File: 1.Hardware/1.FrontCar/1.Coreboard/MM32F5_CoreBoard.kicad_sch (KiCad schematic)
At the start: 74 parts, among them J2 USB-Type-C, J6 SH1.0_2P, U3 CH343P

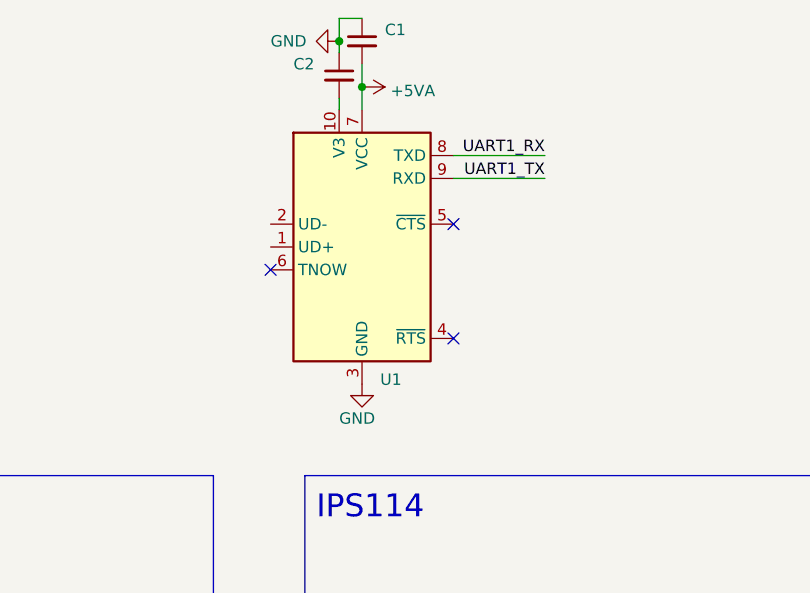
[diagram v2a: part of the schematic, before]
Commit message: 删除遗漏芯片
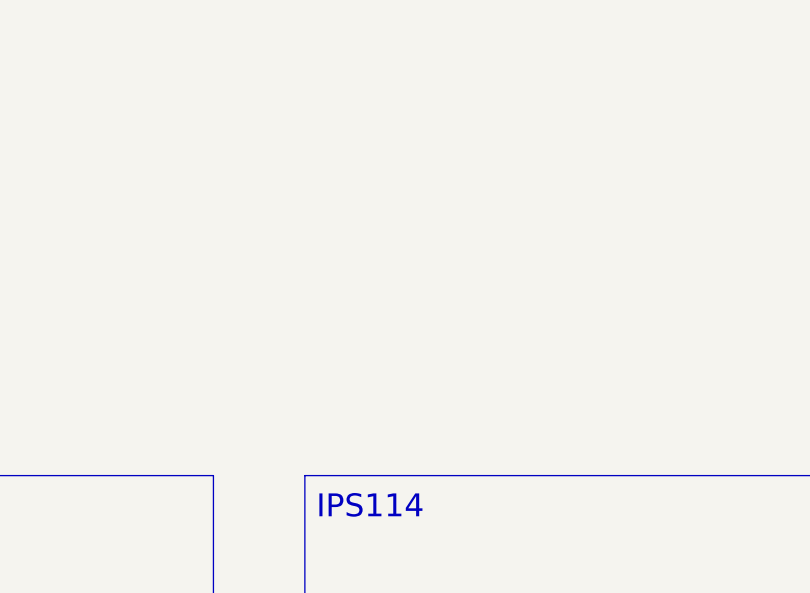
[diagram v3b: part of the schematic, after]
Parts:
- removed C1, C2: (no value), symbol Device:C_Small
- removed U1: (no value), symbol Interface_USB:CH340E
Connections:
- no-connect marks 23 -> 20
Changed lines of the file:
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@@
   (junction (at 69.85 104.14) (diameter 0) (color 0 0 0 0)
   )
-  (junction (at 293.37 -26.67) (diameter 0) (color 0 0 0 0)
-  )
   (junction (at 53.34 30.48) (diameter 0) (color 0 0 0 0)
   )
@@
   (junction (at 85.09 127) (diameter 0) (color 0 0 0 0)
   )
-  (junction (at 290.83 -31.75) (diameter 0) (color 0 0 0 0)
-  )
   (junction (at 193.04 45.72) (diameter 0) (color 0 0 0 0)
   )
@@
   (no_connect (at 95.25 238.76))
   (no_connect (at 95.25 246.38))
-  (no_connect (at 303.53 1.27))
-  (no_connect (at 303.53 -11.43))
   (no_connect (at 257.81 53.34))
   (no_connect (at 160.02 39.37))
@@
   (no_connect (at 160.02 48.26))
   (no_connect (at 257.81 44.45))
-  (no_connect (at 283.21 -6.35))
   (wire (pts (xy 190.5 260.35) (xy 186.69 260.35))
     (stroke (width 0) (type default) (color 0 0 0 0))
@@
     (stroke (width 0) (type default) (color 0 0 0 0))
   )
-  (wire (pts (xy 290.83 -34.29) (xy 293.37 -34.29))
-    (stroke (width 0) (type default) (color 0 0 0 0))
-  )
   (polyline (pts (xy 20.32 139.7) (xy 135.89 139.7))
     (stroke (width 0) (type default) (color 0 0 0 0))
@@
     (stroke (width 0) (type default) (color 0 0 0 0))
   )
-  (wire (pts (xy 290.83 -30.48) (xy 290.83 -31.75))
-    (stroke (width 0) (type default) (color 0 0 0 0))
-  )
   (wire (pts (xy 264.16 255.27) (xy 264.16 254))
     (stroke (width 0) (type default) (color 0 0 0 0))
@@
     (stroke (width 0) (type default) (color 0 0 0 0))
   )
-  (wire (pts (xy 293.37 -26.67) (xy 293.37 -24.13))
-    (stroke (width 0) (type default) (color 0 0 0 0))
-  )
   (wire (pts (xy 251.46 85.09) (xy 251.46 97.79))
     (stroke (width 0) (type default) (color 0 0 0 0))
@@
     (stroke (width 0) (type default) (color 0 0 0 0))
   )
-  (wire (pts (xy 290.83 -25.4) (xy 290.83 -24.13))
-    (stroke (width 0) (type default) (color 0 0 0 0))
-  )
   (wire (pts (xy 157.48 181.61) (xy 156.21 181.61))
     (stroke (width 0) (type default) (color 0 0 0 0))
@@
     (stroke (width 0) (type default) (color 0 0 0 0))
   )
-  (wire (pts (xy 290.83 -31.75) (xy 290.83 -34.29))
-    (stroke (width 0) (type default) (color 0 0 0 0))
-  )
   (wire (pts (xy 49.53 101.6) (xy 49.53 104.14))
     (stroke (width 0) (type default) (color 0 0 0 0))
@@
     (stroke (width 0) (type default) (color 0 0 0 0))
   )
-  (wire (pts (xy 303.53 -19.05) (xy 313.69 -19.05))
-    (stroke (width 0) (type default) (color 0 0 0 0))
-  )
   (polyline (pts (xy 135.89 16.51) (xy 20.32 16.51))
     (stroke (width 0) (type default) (color 0 0 0 0))
@@
     (stroke (width 0) (type default) (color 0 0 0 0))
   )
-  (wire (pts (xy 293.37 -29.21) (xy 293.37 -26.67))
-    (stroke (width 0) (type default) (color 0 0 0 0))
-  )
   (wire (pts (xy 254 204.47) (xy 254 201.93))
     (stroke (width 0) (type default) (color 0 0 0 0))
@@
     (stroke (width 0) (type default) (color 0 0 0 0))
   )
-  (wire (pts (xy 303.53 -16.51) (xy 313.69 -16.51))
-    (stroke (width 0) (type default) (color 0 0 0 0))
-  )
   (wire (pts (xy 269.24 168.91) (xy 266.7 168.91))
     (stroke (width 0) (type default) (color 0 0 0 0))
@@
     (effects (font (size 1.27 1.27)) (justify right bottom))
   )
-  (label "UART1_TX" (at 313.69 -16.51 180)
-    (effects (font (size 1.27 1.27)) (justify right bottom))
-  )
   (label "IPS_BLK" (at 298.45 45.72 0)
     (effects (font (size 1.27 1.27)) (justify left bottom))
@@
     (effects (font (size 1.27 1.27)) (justify right bottom))
   )
-  (label "UART1_RX" (at 313.69 -19.05 180)
-    (effects (font (size 1.27 1.27)) (justify right bottom))
-  )
   (label "IPS_DC" (at 354.33 39.37 0)
     (effects (font (size 1.27 1.27)) (justify left bottom))
@@
     (pin "2")
   )
-  (symbol (lib_id "power:GND") (at 293.37 6.35 0) (unit 1)
-    (in_bom yes) (on_board yes)
-    (property "Reference" "#PWR03" (id 0) (at 293.37 12.7 0)
-      (effects (font (size 1.27 1.27)) hide)
-    )
-    (property "Value" "GND" (id 1) (at 290.83 10.16 0)
-      (effects (font (size 1.27 1.27)) (justify left))
-    )
-    (property "Footprint" "" (id 2) (at 293.37 6.35 0)
-      (effects (font (size 1.27 1.27)) hide)
-    )
-    (property "Datasheet" "" (id 3) (at 293.37 6.35 0)
-      (effects (font (size 1.27 1.27)) hide)
-    )
-    (pin "1")
-  )
   (symbol (lib_id "Device:C_Small") (at 49.53 99.06 180) (unit 1)
     (in_bom yes) (on_board yes)
@@
     (pin "1")
   )
-  (symbol (lib_id "Device:C_Small") (at 293.37 -31.75 0) (unit 1)
-    (in_bom yes) (on_board yes)
-    (property "Reference" "C1" (id 0) (at 295.91 -33.02 0)
-      (effects (font (size 1.27 1.27)) (justify left))
-    )
-    (property "Value" "" (id 1) (at 295.91 -30.48 0)
-      (effects (font (size 1.27 1.27)) (justify left))
-    )
-    (property "Footprint" "" (id 2) (at 293.37 -31.75 0)
-      (effects (font (size 1.27 1.27)) hide)
-    )
-    (property "Datasheet" "~" (id 3) (at 293.37 -31.75 0)
-      (effects (font (size 1.27 1.27)) hide)
-    )
-    (pin "1")
-    (pin "2")
-  )
   (symbol (lib_id "power:+3.3V") (at 205.74 204.47 180) (unit 1)
     (in_bom yes) (on_board yes)
@@
     (pin "1")
   )
-  (symbol (lib_id "Device:C_Small") (at 290.83 -27.94 0) (unit 1)
-    (in_bom yes) (on_board yes)
-    (property "Reference" "C2" (id 0) (at 285.75 -29.21 0)
-      (effects (font (size 1.27 1.27)) (justify left))
-    )
-    (property "Value" "" (id 1) (at 283.21 -26.67 0)
-      (effects (font (size 1.27 1.27)) (justify left))
-    )
-    (property "Footprint" "" (id 2) (at 290.83 -27.94 0)
-      (effects (font (size 1.27 1.27)) hide)
-    )
-    (property "Datasheet" "~" (id 3) (at 290.83 -27.94 0)
-      (effects (font (size 1.27 1.27)) hide)
-    )
-    (pin "1")
-    (pin "2")
-  )
   (symbol (lib_id "power:GND") (at 363.22 123.19 0) (unit 1)
     (in_bom yes) (on_board yes) (fields_autoplaced)
@@
     (pin "2")
   )
-  (symbol (lib_id "Interface_USB:CH340E") (at 293.37 -8.89 0) (unit 1)
-    (in_bom yes) (on_board yes) (fields_autoplaced)
-    (property "Reference" "U1" (id 0) (at 295.3894 5.8404 0)
-      (effects (font (size 1.27 1.27)) (justify left))
-    )
-    (property "Value" "" (id 1) (at 295.3894 8.3773 0)
-      (effects (font (size 1.27 1.27)) (justify left))
-    )
-    (property "Footprint" "" (id 2) (at 294.64 5.08 0)
-      (effects (font (size 1.27 1.27)) (justify left) hide)
-    )
-    (property "Datasheet" "https://www.mpja.com/download/35227cpdata.pdf" (id 3) (at 284.48 -29.21 0)
-      (effects (font (size 1.27 1.27)) hide)
-    )
-    (pin "1")
-    (pin "10")
-    (pin "2")
-    (pin "3")
-    (pin "4")
-    (pin "5")
-    (pin "6")
-    (pin "7")
-    (pin "8")
-    (pin "9")
-  )
   (symbol (lib_id "power:+5VA") (at 78.74 36.83 90) (unit 1)
     (in_bom yes) (on_board yes)
@@
     (pin "9")
   )
-  (symbol (lib_id "power:+5VA") (at 293.37 -26.67 270) (unit 1)
-    (in_bom yes) (on_board yes) (fields_autoplaced)
-    (property "Reference" "#PWR02" (id 0) (at 289.56 -26.67 0)
-      (effects (font (size 1.27 1.27)) hide)
-    )
-    (property "Value" "+5VA" (id 1) (at 296.545 -26.2362 90)
-      (effects (font (size 1.27 1.27)) (justify left))
-    )
-    (property "Footprint" "" (id 2) (at 293.37 -26.67 0)
-      (effects (font (size 1.27 1.27)) hide)
-    )
-    (property "Datasheet" "" (id 3) (at 293.37 -26.67 0)
-      (effects (font (size 1.27 1.27)) hide)
-    )
-    (pin "1")
-  )
   (symbol (lib_id "Device:R_Small") (at 194.31 57.15 90) (unit 1)
     (in_bom yes) (on_board yes)
@@
     (pin "2")
   )
-  (symbol (lib_id "power:GND") (at 290.83 -31.75 270) (unit 1)
-    (in_bom yes) (on_board yes)
-    (property "Reference" "#PWR01" (id 0) (at 284.48 -31.75 0)
-      (effects (font (size 1.27 1.27)) hide)
-    )
-    (property "Value" "GND" (id 1) (at 283.21 -31.75 90)
-      (effects (font (size 1.27 1.27)) (justify left))
-    )
-    (property "Footprint" "" (id 2) (at 290.83 -31.75 0)
-      (effects (font (size 1.27 1.27)) hide)
-    )
-    (property "Datasheet" "" (id 3) (at 290.83 -31.75 0)
-      (effects (font (size 1.27 1.27)) hide)
-    )
-    (pin "1")
-  )
   (symbol (lib_id "power:+3.3V") (at 74.93 227.33 90) (unit 1)
     (in_bom yes) (on_board yes)
@@
   )
   (symbol_instances
-    (path "/eb4d6e48-edf1-44f1-9e33-5c87081bce1d"
-      (reference "#PWR01") (unit 1) (value "GND") (footprint "")
-    )
-    (path "/de50920c-1290-471f-a298-f5182d5a82db"
-      (reference "#PWR02") (unit 1) (value "+5VA") (footprint "")
-    )
-    (path "/2bc1e854-4639-415d-bc23-e2702d2a4ad5"
-      (reference "#PWR03") (unit 1) (value "GND") (footprint "")
-    )
     (path "/18ee732d-2cd1-412e-81ae-c983b3f87517"
       (reference "#PWR04") (unit 1) (value "+3.3V") (footprint "")
@@
       (reference "#PWR079") (unit 1) (value "GND") (footprint "")
     )
-    (path "/3d80c7a9-22a4-40e2-b1e6-b9ddf890a9cb"
-      (reference "C1") (unit 1) (value "100nF") (footprint "ErBW_s:C_0402")
-    )
-    (path "/98203549-e80b-49c8-8284-ee30a1ded8a5"
-      (reference "C2") (unit 1) (value "100nF") (footprint "ErBW_s:C_0402")
-    )
     (path "/4dcfdf7a-a544-4854-9ee7-14569f884c7d"
       (reference "C3") (unit 1) (value "100nF") (footprint "ErBW_s:C_0402")
@@
       (reference "SW4") (unit 1) (value "3x4") (footprint "ErBW_s:BUTTON_3x4")
     )
-    (path "/9f9d1f6f-7507-4bd1-b7c3-1eb7cae036e5"
-      (reference "U1") (unit 1) (value "CH340E") (footprint "Package_SO:MSOP-10_3x3mm_P0.5mm")
-    )
     (path "/44e26f84-2654-4077-bd63-b4366d7865c2"

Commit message: Normal updates
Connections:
- net GND: now also D2.2 (A); no longer D2.1 (K)
- net at R7.2: now also D2.1 (K); no longer D2.2 (A)
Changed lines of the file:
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@@
   (symbol (lib_id "Device:R_Small") (at 119.38 170.18 0) (unit 1)
     (in_bom yes) (on_board yes)
-    (property "Reference" "R14" (id 0) (at 115.57 168.91 0)
+    (property "Reference" "R14" (id 0) (at 114.3 168.91 0)
       (effects (font (size 1.27 1.27)) (justify left))
     )
@@
   )
   (symbol (lib_id "Device:LED_Small") (at 101.6 55.88 180) (unit 1)
-    (in_bom yes) (on_board yes) (fields_autoplaced)
-    (property "Reference" "D2" (id 0) (at 101.5365 51.1642 0))
-    (property "Value" "" (id 1) (at 101.5365 53.7011 0))
+    (in_bom yes) (on_board yes)
+    (property "Reference" "D2" (id 0) (at 101.6 50.8 0))
+    (property "Value" "" (id 1) (at 101.6 53.34 0))
     (property "Footprint" "" (id 2) (at 101.6 55.88 90)
       (effects (font (size 1.27 1.27)) hide)
@@
     (in_bom yes) (on_board yes)
     (property "Reference" "C34" (id 0) (at 100.33 256.54 90))
-    (property "Value" "" (id 1) (at 104.14 256.54 90))
+    (property "Value" "" (id 1) (at 105.41 256.54 90))
     (property "Footprint" "" (id 2) (at 101.6 254 0)
       (effects (font (size 1.27 1.27)) hide)
@@
     )
     (path "/e7147057-bc49-420f-bd99-5e1755617994"
-      (reference "C27") (unit 1) (value "18pF") (footprint "ErBW_s:C_0402")
+      (reference "C27") (unit 1) (value "100nF") (footprint "ErBW_s:C_0402")
     )
     (path "/9f918f34-55ed-4af1-9818-488ac007d9d8"

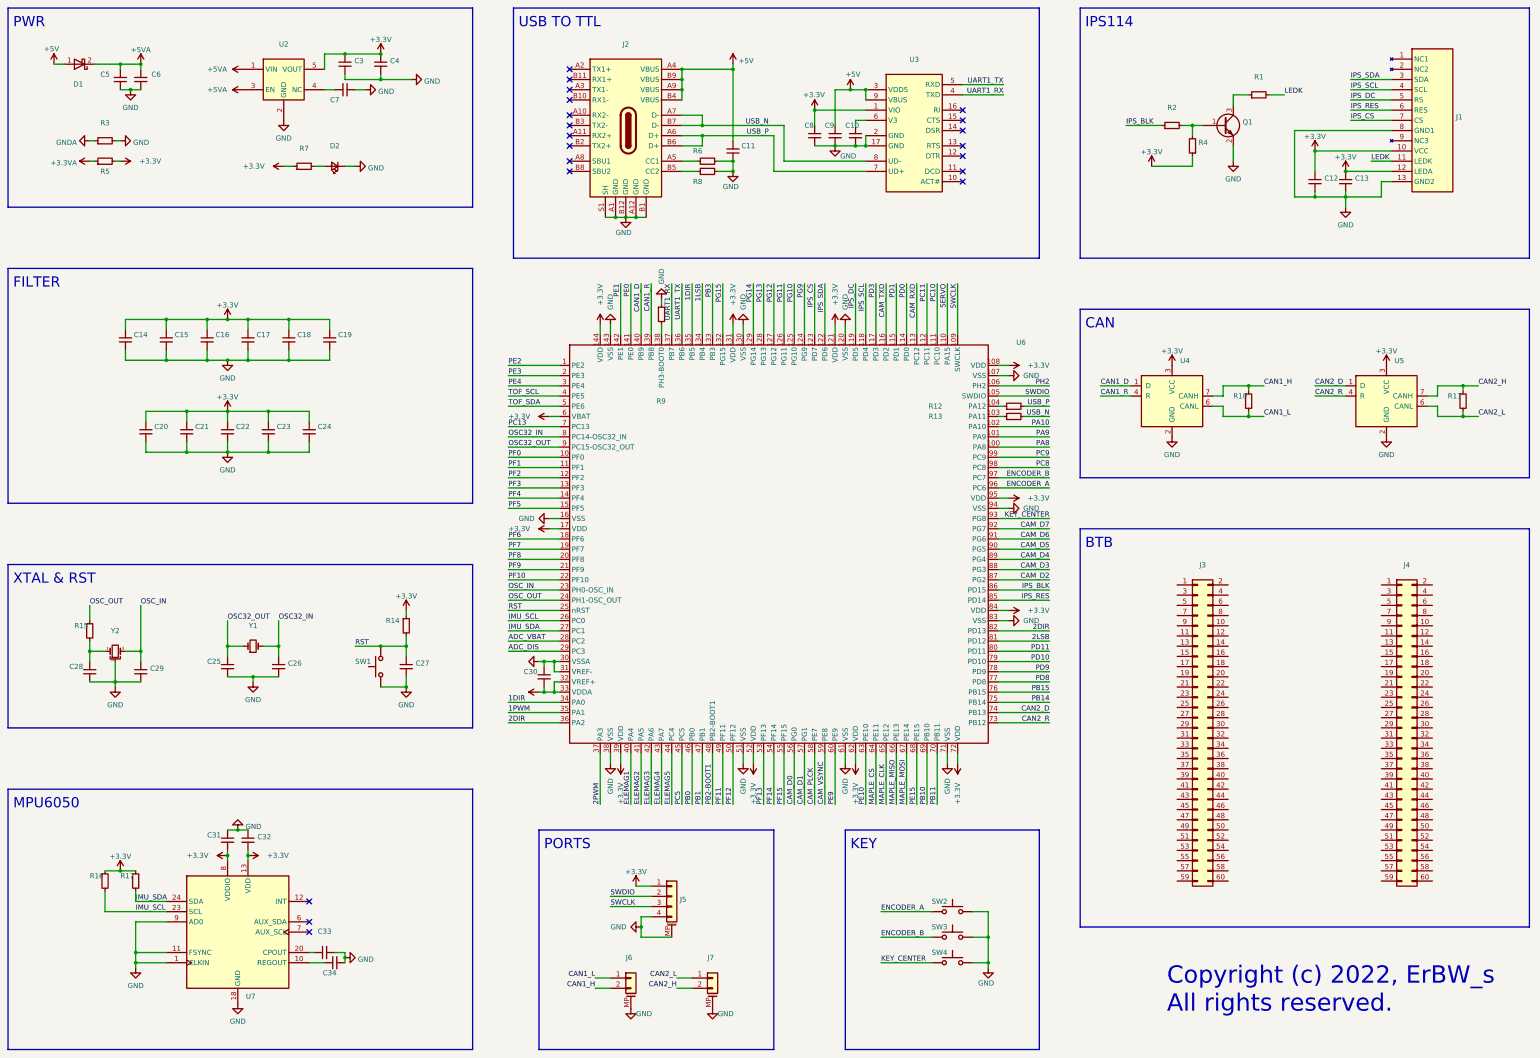
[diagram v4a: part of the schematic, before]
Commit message: 删除ips背光三极管，改为直接接地
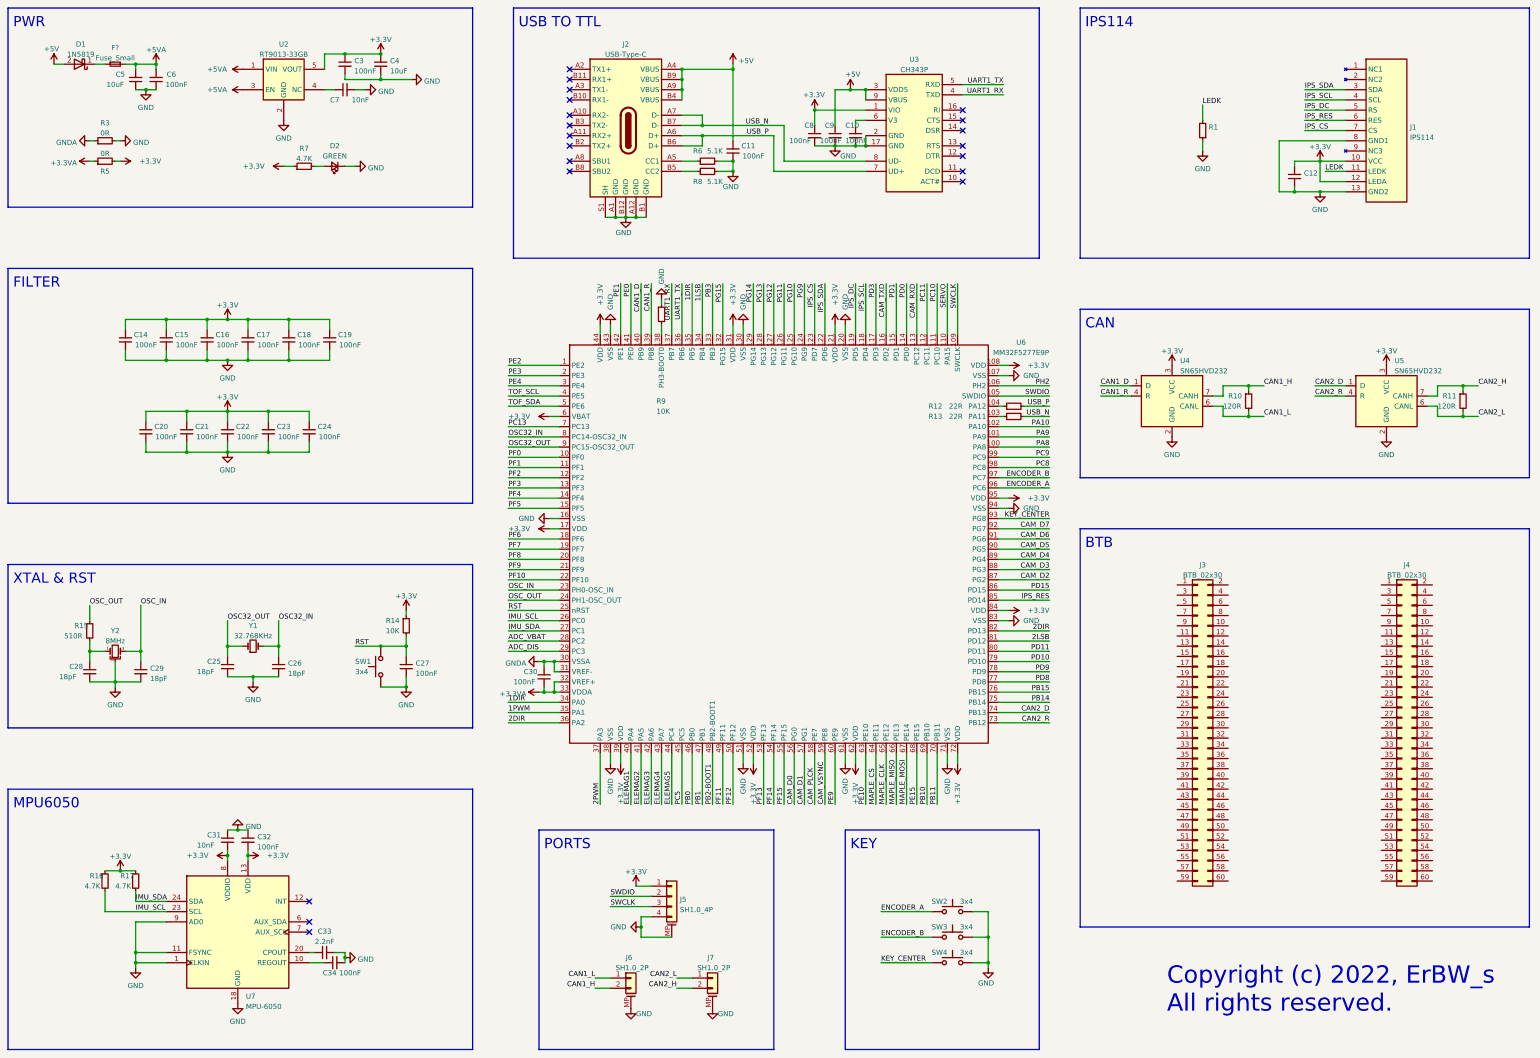
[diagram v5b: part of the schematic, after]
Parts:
- removed C13: (no value), symbol Device:C_Small
- removed Q1: (no value), symbol Device:Q_NPN_BEC
- removed R2, R4: (no value), symbol Device:R_Small
- added F?: Fuse_Small, symbol Device:Fuse_Small
- C10, C11, C14, C15, C16, C17, C18, C19, C20, C21, C22, C23, C24, C27, C3, C30, C32, C34, C6, C8, C9: value (none) -> 100nF; footprint (none) -> ErBW_s:C_0402
- C12: footprint (none) -> ErBW_s:C_0402
- C25, C26, C28, C29: value (none) -> 18pF; footprint (none) -> ErBW_s:C_0402
- C31, C7: value (none) -> 10nF; footprint (none) -> ErBW_s:C_0402
- C33: value (none) -> 2.2nF; footprint (none) -> ErBW_s:C_0402
- C4, C5: value (none) -> 10uF; footprint (none) -> ErBW_s:C_0402
- D1: value (none) -> 1N5819; footprint (none) -> ErBW_s:SOD-323
- D2: value (none) -> GREEN; footprint (none) -> ErBW_s:LED_0402
- J1: value (none) -> IPS114; footprint (none) -> ErBW_s:IPS114
- J3, J4: value (none) -> BTB_02x30; footprint (none) -> ErBW_s:BTB_Connector_02x30
- J5: value (none) -> SH1.0_4P; footprint (none) -> Connector_JST:JST_SH_SM04B-SRSS-TB_1x04-1MP_P1.00mm_Horizontal
- J7: value (none) -> SH1.0_2P; footprint (none) -> Connector_JST:JST_SH_SM02B-SRSS-TB_1x02-1MP_P1.00mm_Horizontal
- R1: footprint (none) -> ErBW_s:R_0402
- R10, R11: value (none) -> 120R; footprint (none) -> ErBW_s:R_0402
- R12, R13: value (none) -> 22R; footprint (none) -> ErBW_s:R_0402
- R14, R9: value (none) -> 10K; footprint (none) -> ErBW_s:R_0402
- R15: value (none) -> 510R; footprint (none) -> ErBW_s:R_0402
- R16, R17, R7: value (none) -> 4.7K; footprint (none) -> ErBW_s:R_0402
- R3, R5: value (none) -> 0R; footprint (none) -> ErBW_s:R_0402
- R6, R8: value (none) -> 5.1K; footprint (none) -> ErBW_s:R_0402
- SW1, SW2, SW3, SW4: value (none) -> 3x4; footprint (none) -> ErBW_s:BUTTON_3x4
- U2: value (none) -> RT9013-33GB; footprint (none) -> Package_TO_SOT_SMD:SOT-23-5
- U4, U5: value (none) -> SN65HVD232; footprint (none) -> Package_SO:SOIC-8_3.9x4.9mm_P1.27mm
- U6: value (none) -> MM32F5277E9P; footprint (none) -> Package_QFP:LQFP-144_20x20mm_P0.5mm
- U7: value (none) -> MPU-6050; footprint (none) -> Sensor_Motion:InvenSense_QFN-24_4x4mm_P0.5mm
- Y1: value (none) -> 32.768KHz; footprint (none) -> ErBW_s:Crystal_SMD_3215_FC-135_2P
- Y2: value (none) -> 8MHz; footprint (none) -> ErBW_s:Crystal_SMD_3213_3P
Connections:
- net +5V: now also D1.2 (A); no longer D1.1 (K)
- net +5VA: now also F?.2; no longer D1.2 (A)
- net GND: now also R1.1
- net IPS_BLK renamed PD15
- new net: D1.1 (K), F?.1
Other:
- moved on the sheet: C12, C5, C6, J1, R1
